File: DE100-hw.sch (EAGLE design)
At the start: 50 parts, among them IC3 74HC14D, IC4 74HC14D, U1 TLP521-4(GB), U2 TLP521-4(GB), X4 JST-XH-10-PIN-LONG-PAD, X5 JST-XH-04-PIN-LONG-PAD, X6 JST-XH-03-PIN-LONG-PAD

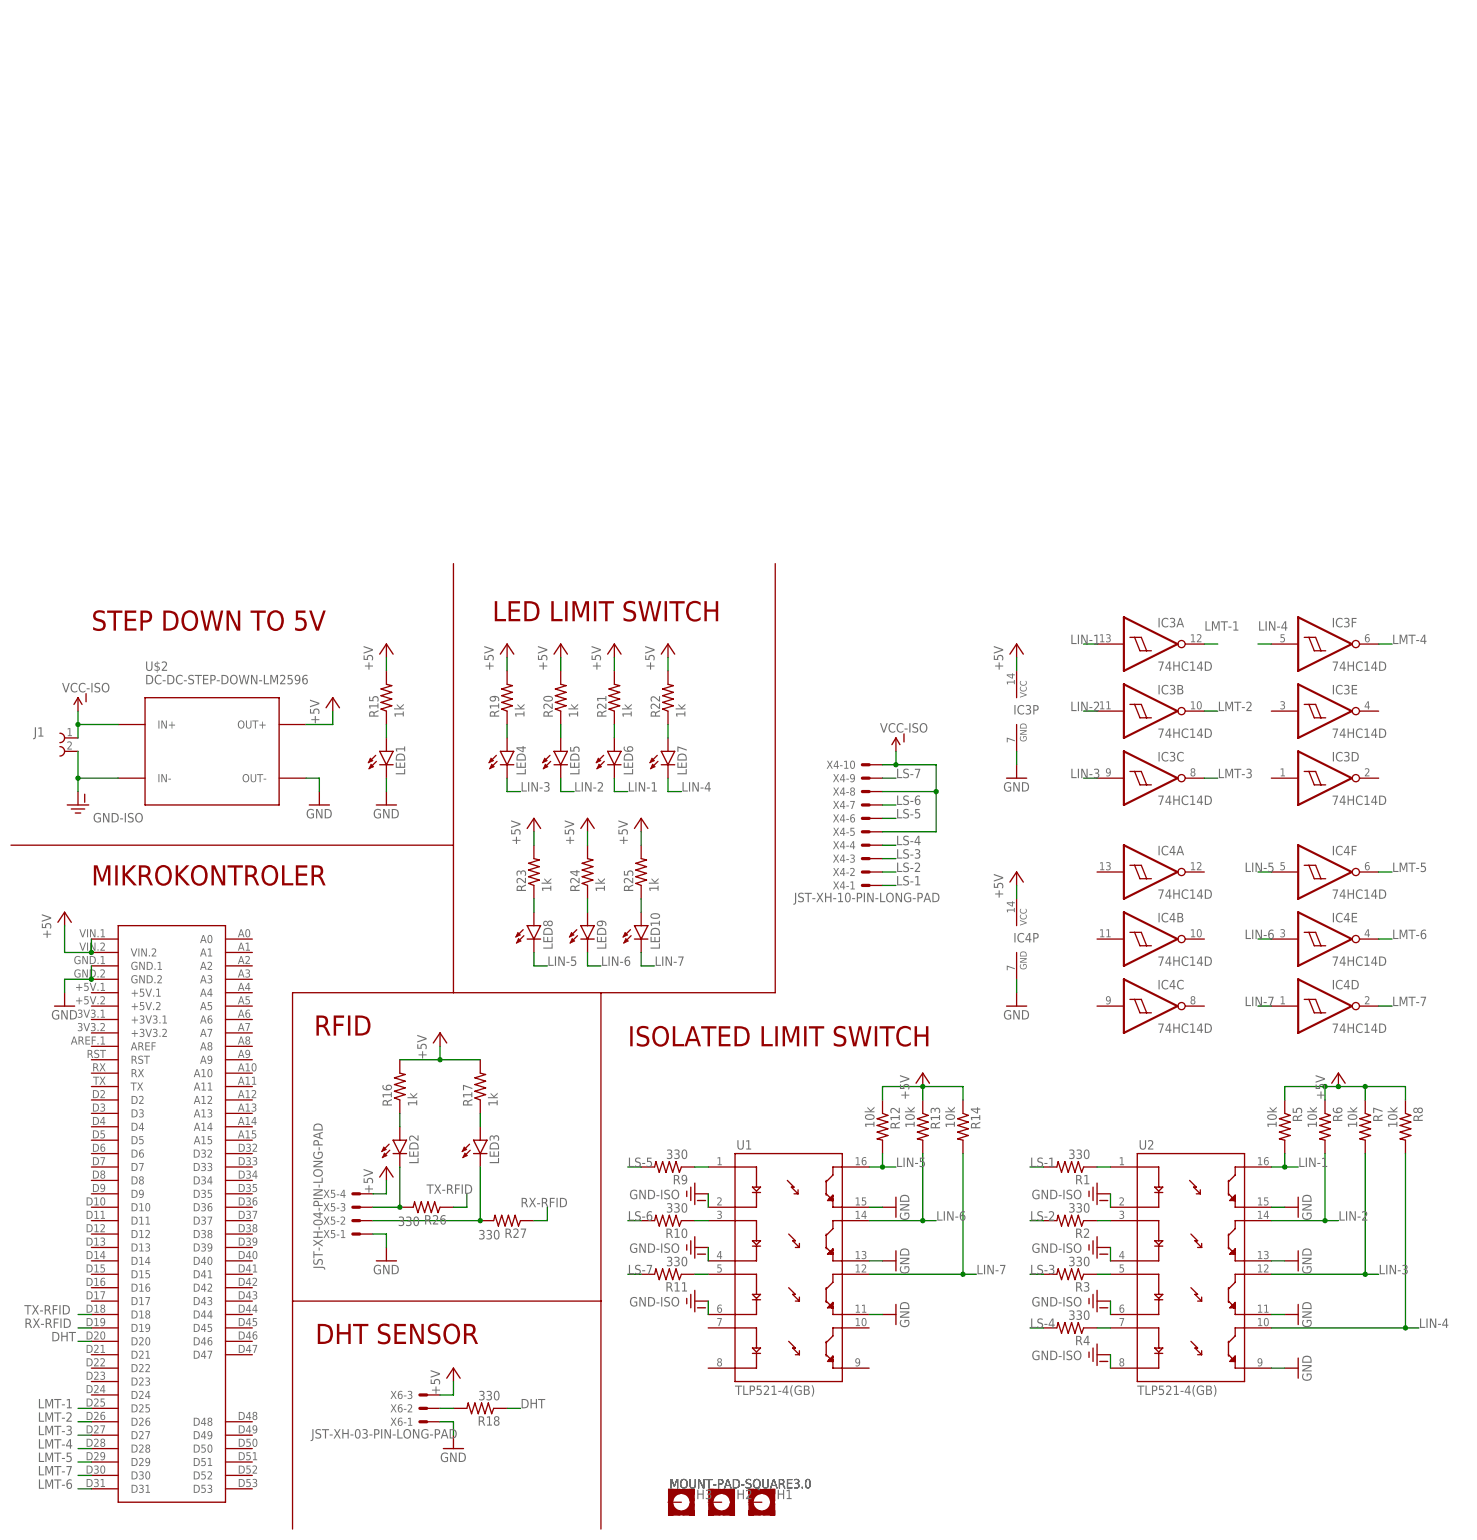
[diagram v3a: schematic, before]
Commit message: add power protection
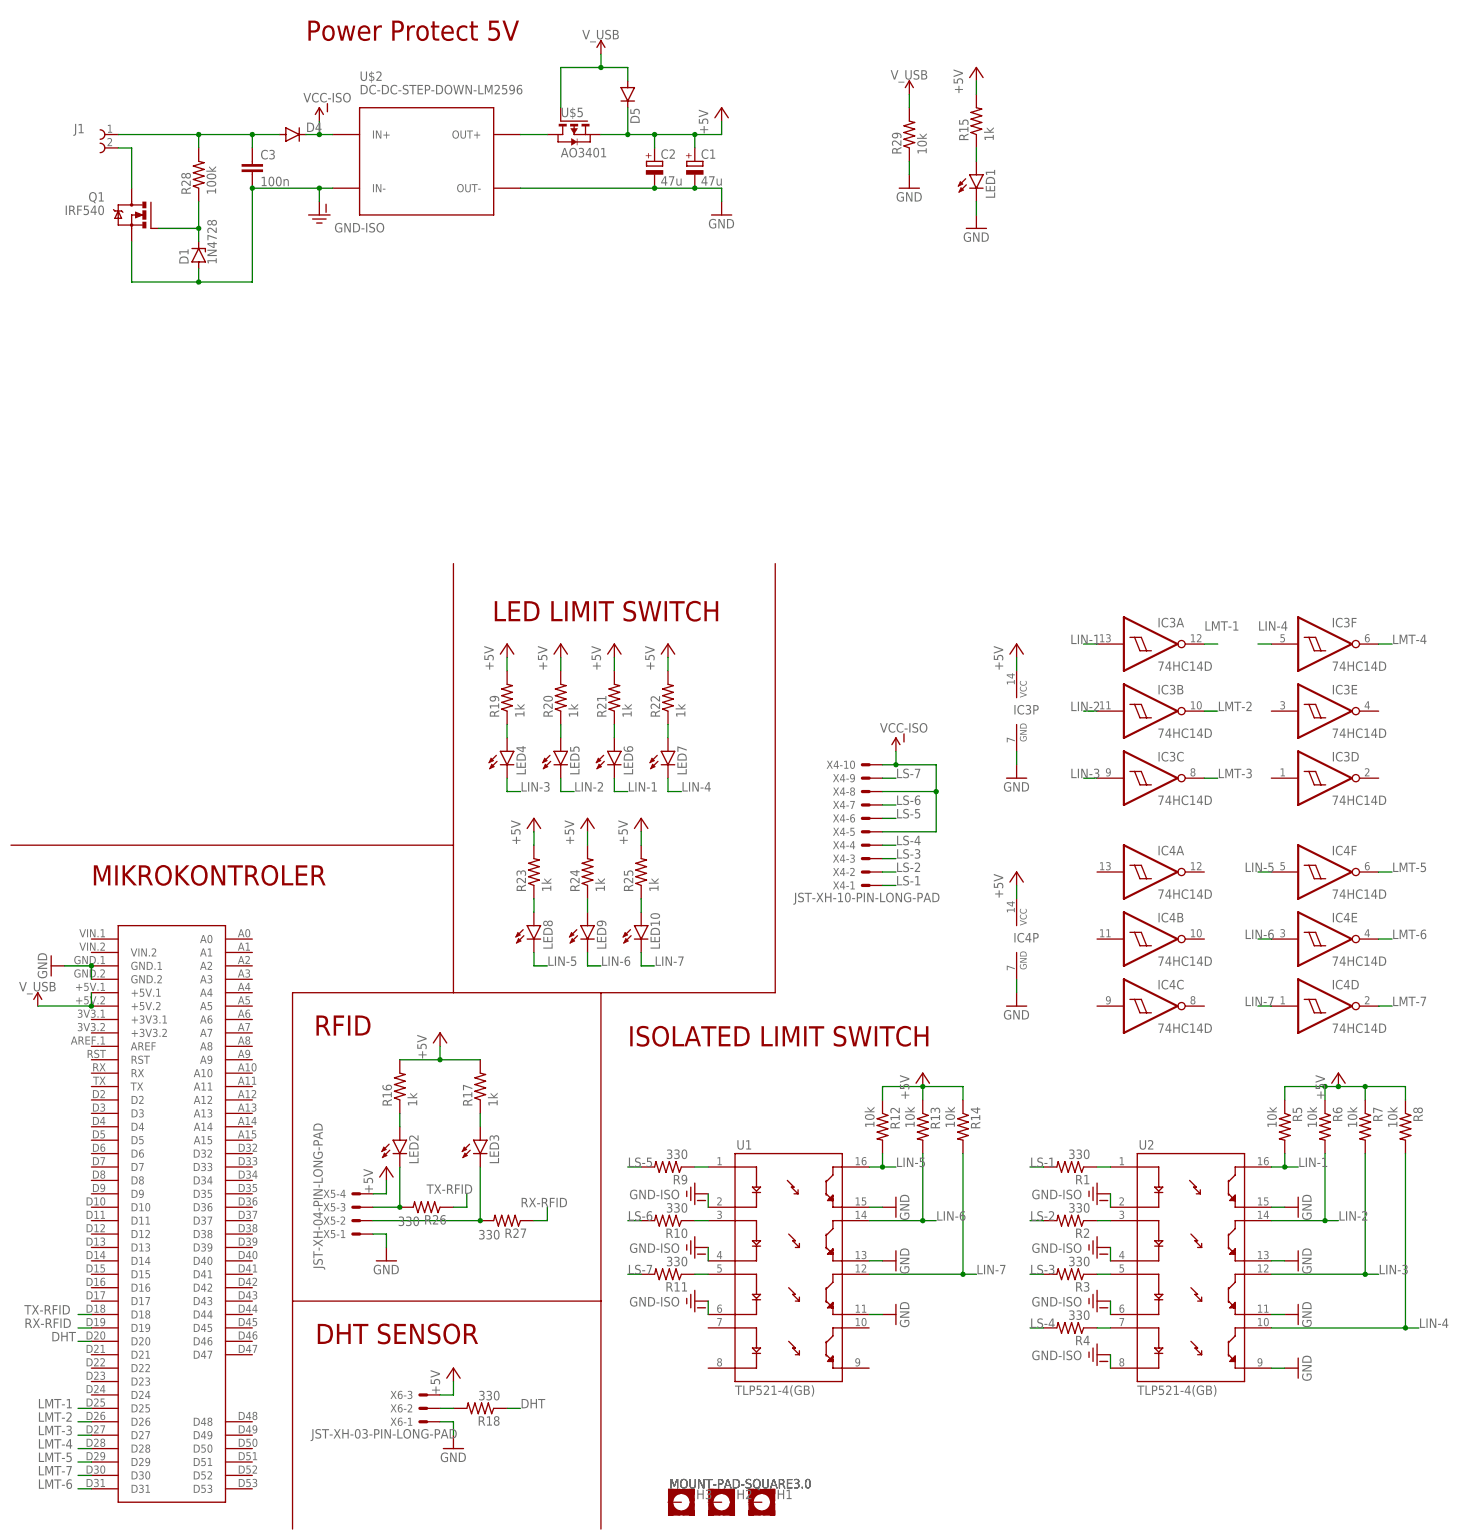
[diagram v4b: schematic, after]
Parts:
- added C1, C2: 47u, rcl:CPOL-EUUD-6,3X8,8
- added C3: 100n, rcl:C-EUC0805K
- added D1: 1N4728, diode:1N4728
- added D4, D5: (no value), diode:DIODE-DO-214AC
- added Q1: IRF540, transistor-power:IRF540
- added R28: 100k, rcl:R-US_R0805
- added R29: 10k, rcl:R-US_R0805
- added U$5: AO3401, AO3401:AO3401
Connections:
- new net N$1: J1.2, Q1.D
- new net N$2: U$2.OUT+, U$5.D
- new net N$3: D1.C, Q1.G, R28.1
- new net N$4: C3.1, D4.A, J1.1, R28.2
- new net V_USB: D5.A, R29.2, U$1.+5V.1, U$1.+5V.2, U$5.G
- net +5V: now also C1.+, C2.+, D5.C, U$5.S; no longer U$1.VIN.1, U$1.VIN.2, U$2.OUT+
- net GND: now also C1.-, C2.-, R29.1
- net GND-ISO: now also C3.2, D1.A, Q1.S; no longer J1.2
- net VCC-ISO: now also D4.C; no longer J1.1
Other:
- note added: "Power Protect 5V"
- note removed: "STEP DOWN TO 5V"
- moved on the sheet: J1, LED1, R15, U$2
